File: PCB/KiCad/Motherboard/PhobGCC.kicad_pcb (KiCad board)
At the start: 2 copper layers, 125.5 x 72.9 mm, 67 parts, among them J1 Conn_01x06_Female, J2 Conn_01x04_Female, J3 Conn_01x01_Male, J5 Conn_01x02_Male, Q1 Q_NMOS_GSD, Q2 Q_PMOS_GDS, Q3 Q_NMOS_GSD, SW1 A, SW10 Dup, SW11 Dright, SW12 Ddown, SW2 B, SW3 X, SW4 Y, SW5 Start, SW6 L, SW7 R, SW8 Z, SW9 Dleft, U1 Teensy4.0, U2 2x DRV5053CAQLPGM Hall Effect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, U3 GP2S60-MFG, U4 GP2S60-MFG

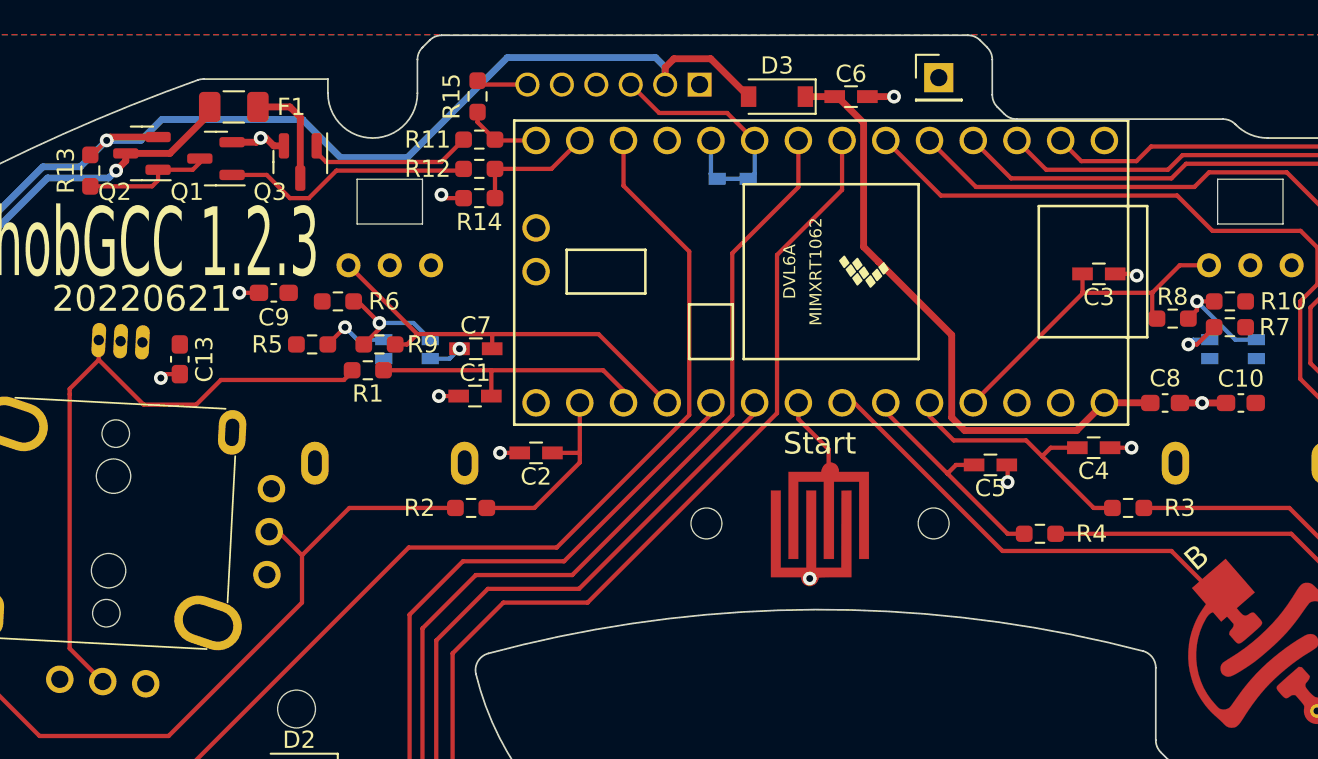
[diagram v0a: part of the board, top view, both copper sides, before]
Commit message: Replaced teensy 4 with pico stamp and completed basic schematic and layout changes
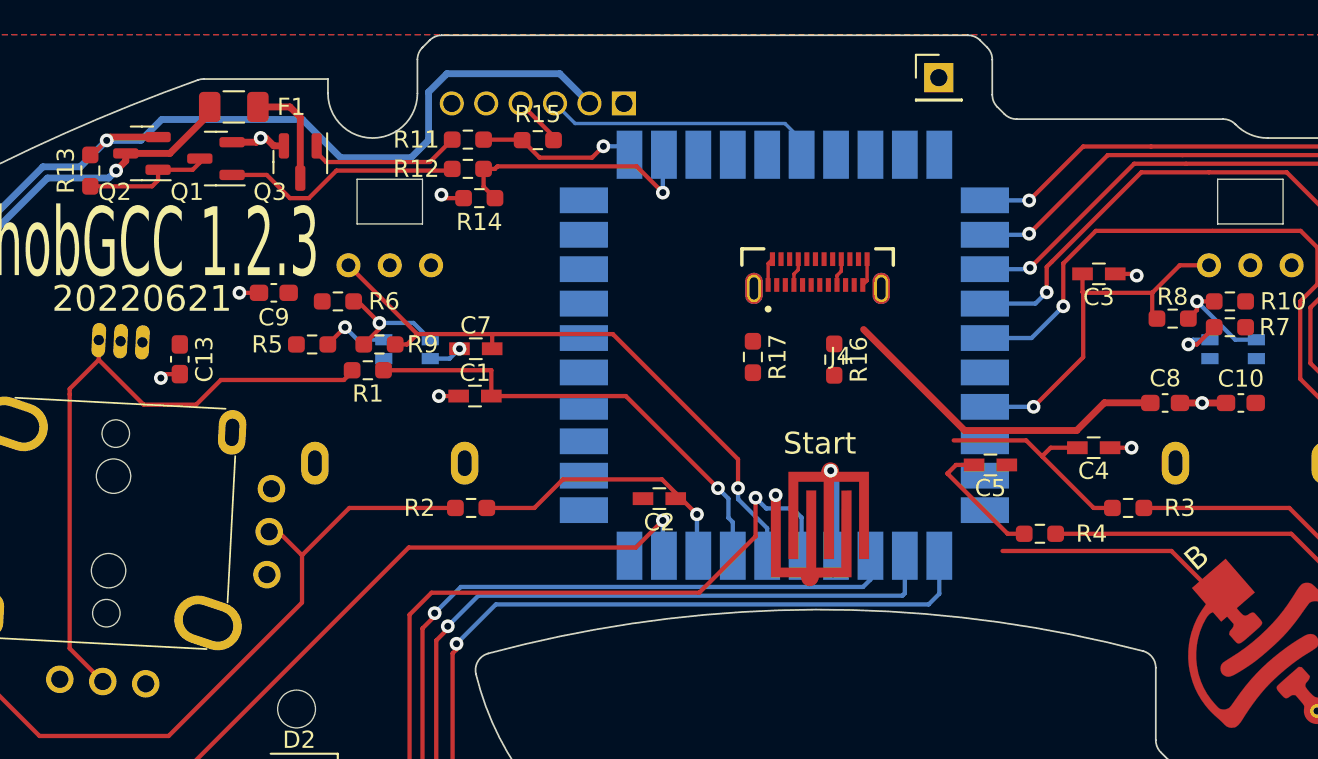
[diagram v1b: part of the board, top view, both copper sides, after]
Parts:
- removed C6: 10u, PhobGCC_Footprints:C_0603_HandSoldering
- removed D1: D_Schottky_Shorted, PhobGCC_Footprints:D_SOD-523_Shorted
- removed D3: M7C, PhobGCC_Footprints:D_SOD-123
- removed H5, H6: 1.8mm, PhobGCC_Footprints:MountingHole_1.8mm
- removed U1: Teensy4.0, PhobGCC_Footprints:Teensy40_Edge_Pins
- added J4: USB_C_Receptacle_USB2.0, USB4155-03-C_REVA:GCT_USB4155-03-C_REVA, F.Cu at (111.2, 37.3)
- added R16: R_Small, Resistor_SMD:R_0603_1608Metric_Pad0.98x0.95mm_HandSolder, F.Cu at (112.1, 42.4)
- added R17: R_Small, Resistor_SMD:R_0603_1608Metric_Pad0.98x0.95mm_HandSolder, F.Cu at (107.4, 42.3)
- added U5: RP2040_Stamp, RP2040_Stamp:RP2040_Stamp_SMD, B.Cu at (109.2, 42.2)
- moved C2 7.64 mm to (102.0, 50.5)
- moved J1 4.53 mm to (99.9, 27.5)
- moved R15 4.33 mm to (94.9, 29.7), turned to 180 degrees
- moved R11 0.66 mm to (90.8, 29.6)
- moved R12 0.66 mm to (90.8, 31.3)
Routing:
- net /L: track 72.1 -> 52.6 mm, vias 0 -> 1
- net Net-(C6-Pad1): track 35.5 -> 19.7 mm
- net /B: track 26.8 -> 13.9 mm
- net /Ddown: track 74.7 -> 62.7 mm, vias 0 -> 1
- net /Lanalog: track 24.2 -> 36.0 mm, vias 0 -> 1
- net /Stick_x_filt: track 16.7 -> 27.5 mm, vias 0 -> 1
- net /Dright: track 64.2 -> 54.3 mm, vias 0 -> 1
- net /Brake: track 7.30 -> 15.3 mm, vias 0 -> 1
- net +5V: track 131.4 -> 124.0 mm
- net /Dup: track 40.5 -> 47.2 mm, vias 0 -> 1
- net /Dleft: track 47.2 -> 53.8 mm, vias 0 -> 1
- net /C_y_filt: track 12.8 -> 7.76 mm
- net /Rumble: track 4.36 -> 9.39 mm, vias 0 -> 1
- net /Z: track 37.2 -> 42.1 mm, vias 0 -> 1
- net /Stick_y_filt: track 11.7 -> 16.5 mm, vias 0 -> 1
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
